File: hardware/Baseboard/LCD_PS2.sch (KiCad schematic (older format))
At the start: 3 parts, among them X4 KEYBOARD

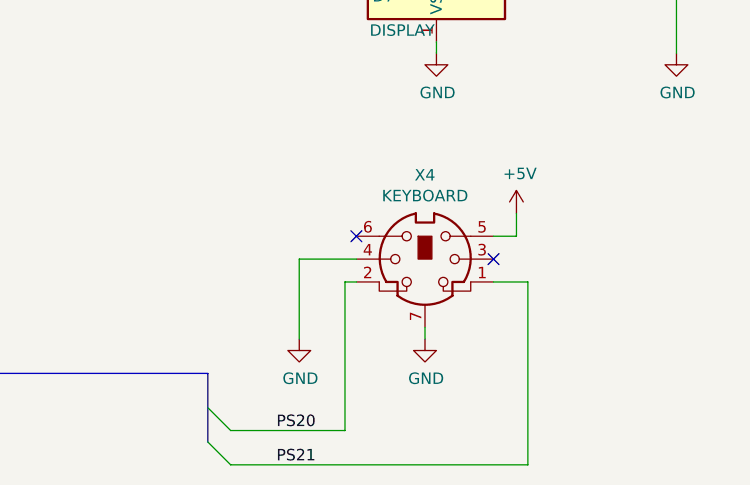
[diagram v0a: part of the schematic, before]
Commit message: Rework hardware for IRQ, change some routing
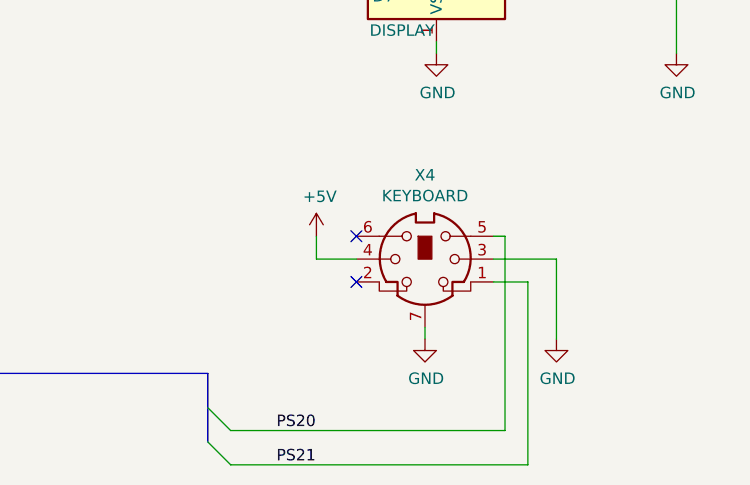
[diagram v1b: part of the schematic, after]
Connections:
- net +5V: now also X4.4; no longer X4.5
- net GND: now also X4.3; no longer X4.4
- net PS20: now also X4.5; no longer X4.2
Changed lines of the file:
@@
 $Descr A4 11693 8268
 encoding utf-8
-Sheet 4 6
+Sheet 4 7
 Title "Baseboard"
-Date ""
-Rev "1.0"
+Date "2019-11-24"
+Rev "1.1"
 Comp "https://www.kampis-elektroecke.de"
 Comment1 "Author: Daniel Kampert"
 Comment2 ""
 Comment3 ""
-Comment4 ""
+Comment4 "LCD & P2/2"
 $EndDescr
 Wire Wire Line
@@
 $EndComp
 $Comp
-L power:GND #PWR?
-U 1 1 5DD59313
-P 5000 5900
-AR Path="/5DD59313" Ref="#PWR?"  Part="1"
-AR Path="/5EB09E21/5DD59313" Ref="#PWR?"  Part="1"
-AR Path="/5DADBF97/5DD59313" Ref="#PWR072"  Part="1"
-F 0 "#PWR072" H 5000 5650 50  0001 C CNN
-F 1 "GND" H 5005 5727 50  0000 C CNN
-F 2 "" H 5000 5900 50  0001 C CNN
-F 3 "" H 5000 5900 50  0001 C CNN
-	1    5000 5900
-	1    0    0    -1
-$EndComp
-Wire Wire Line
-	5250 5550 5000 5550
-Wire Wire Line
-	5000 5550 5000 5900
-Wire Wire Line
-	5850 5450 5950 5450
-$Comp
 L power:+5V #PWR?
 U 1 1 5DD5A54C
-P 5950 5350
+P 5075 5450
 AR Path="/5DD5A54C" Ref="#PWR?"  Part="1"
 AR Path="/5EB09E21/5DD5A54C" Ref="#PWR?"  Part="1"
 AR Path="/5DADBF97/5DD5A54C" Ref="#PWR073"  Part="1"
-F 0 "#PWR073" H 5950 5200 50  0001 C CNN
-F 1 "+5V" H 5965 5523 50  0000 C CNN
-F 2 "" H 5950 5350 50  0001 C CNN
-F 3 "" H 5950 5350 50  0001 C CNN
-	1    5950 5350
-	1    0    0    -1
-$EndComp
-Wire Wire Line
-	5950 5450 5950 5350
+F 0 "#PWR073" H 5075 5300 50  0001 C CNN
+F 1 "+5V" H 5090 5623 50  0000 C CNN
+F 2 "" H 5075 5450 50  0001 C CNN
+F 3 "" H 5075 5450 50  0001 C CNN
+	1    5075 5450
+	1    0    0    -1
+$EndComp
+Wire Wire Line
+	5075 5550 5075 5450
 Entry Wire Line
 	4600 6200 4700 6300
@@
 PS2[0..1]
 Wire Wire Line
-	4700 6300 5200 6300
-Wire Wire Line
-	5200 6300 5200 5650
-Wire Wire Line
-	5200 5650 5250 5650
-Wire Wire Line
 	4700 6450 6000 6450
 Wire Wire Line
@@
 	5850 5650 6000 5650
 NoConn ~ 5250 5450
-NoConn ~ 5850 5550
 Wire Wire Line
 	5600 2900 5600 3000
@@
 	1    0    0    -1
 $EndComp
+$Comp
+L power:GND #PWR?
+U 1 1 5DDCDE4D
+P 6125 5900
+AR Path="/5DDCDE4D" Ref="#PWR?"  Part="1"
+AR Path="/5EB09E21/5DDCDE4D" Ref="#PWR?"  Part="1"
+AR Path="/5DADBF97/5DDCDE4D" Ref="#PWR0103"  Part="1"
+F 0 "#PWR0103" H 6125 5650 50  0001 C CNN
+F 1 "GND" H 6130 5727 50  0000 C CNN
+F 2 "" H 6125 5900 50  0001 C CNN
+F 3 "" H 6125 5900 50  0001 C CNN
+	1    6125 5900
+	1    0    0    -1
+$EndComp
+Wire Wire Line
+	6125 5550 6125 5900
+Wire Wire Line
+	5850 5550 6125 5550
+Wire Wire Line
+	5250 5550 5075 5550
+Wire Wire Line
+	5900 5450 5900 6300
+Wire Wire Line
+	4700 6300 5900 6300
+Wire Wire Line
+	5850 5450 5900 5450
+NoConn ~ 5250 5650
 Wire Bus Line
 	4600 6050 4600 6350

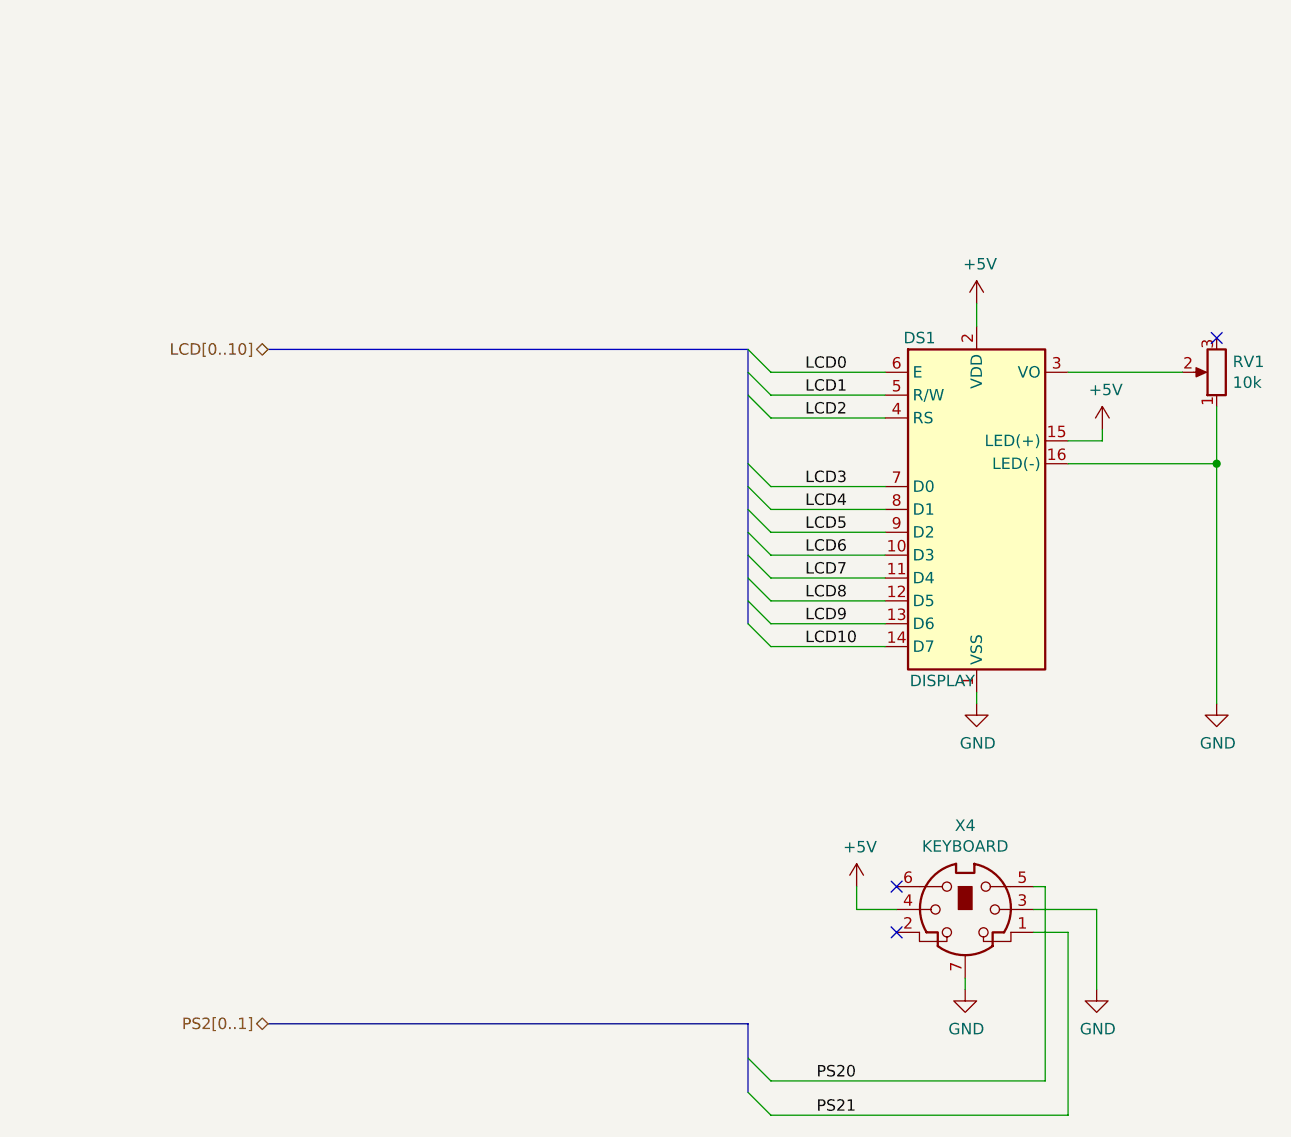
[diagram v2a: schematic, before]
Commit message: Add pull up resistors for PS/2, add LCD backlight switch
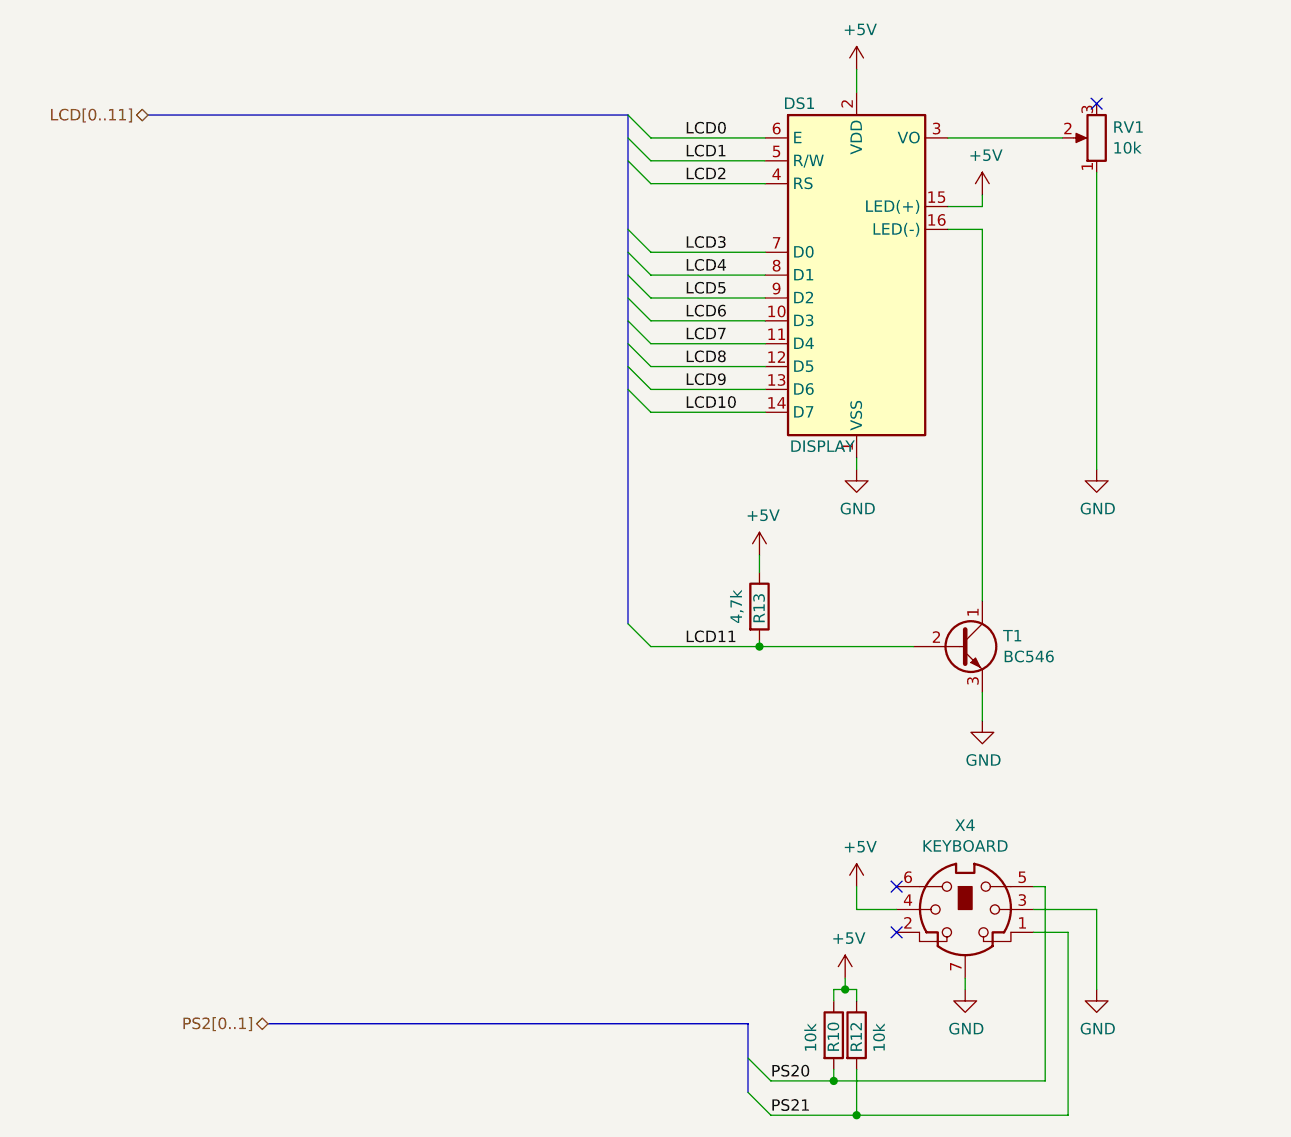
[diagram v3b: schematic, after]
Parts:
- added R10, R12: 10k, Resistor_THT:R_Axial_DIN0207_L6.3mm_D2.5mm_P7.62mm_Horizontal, symbol Device:R
- added R13: 4,7k, Resistor_THT:R_Axial_DIN0207_L6.3mm_D2.5mm_P7.62mm_Horizontal, symbol Device:R
- added T1: BC546, Package_TO_SOT_THT:TO-92_Inline, symbol Transistor_BJT:BC546
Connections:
- net +5V: now also R10.1, R12.1, R13.1
- net GND: now also T1.3 (E); no longer DS1.16 (LED(-))
- net PS20: now also R10.2
- net PS21: now also R12.2
- new net: DS1.16 (LED(-)), T1.1 (C)
- new net LCD11: R13.2, T1.2 (B)
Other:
- moved on the sheet: DS1, RV1
